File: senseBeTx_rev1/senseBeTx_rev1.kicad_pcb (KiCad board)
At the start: 2 copper layers, 40 x 80 mm, 37 parts, among them J1 Audio-Jack-4_1Switches, P1 CONN_02X05, Q1 TSM2301, Q2 Q_NMOS_DGS, Q3 Q_NMOS_DGS, Q4 Q_NMOS_DGS, Q5 Q_NMOS_DGS, Q6 Q_NMOS_DGS, Q7 Q_NMOS_DGS, Q8 Q_NMOS_DGS, SW1 SW_Push_Dual, U1 STM32L011F3Px, Y1 Crystal

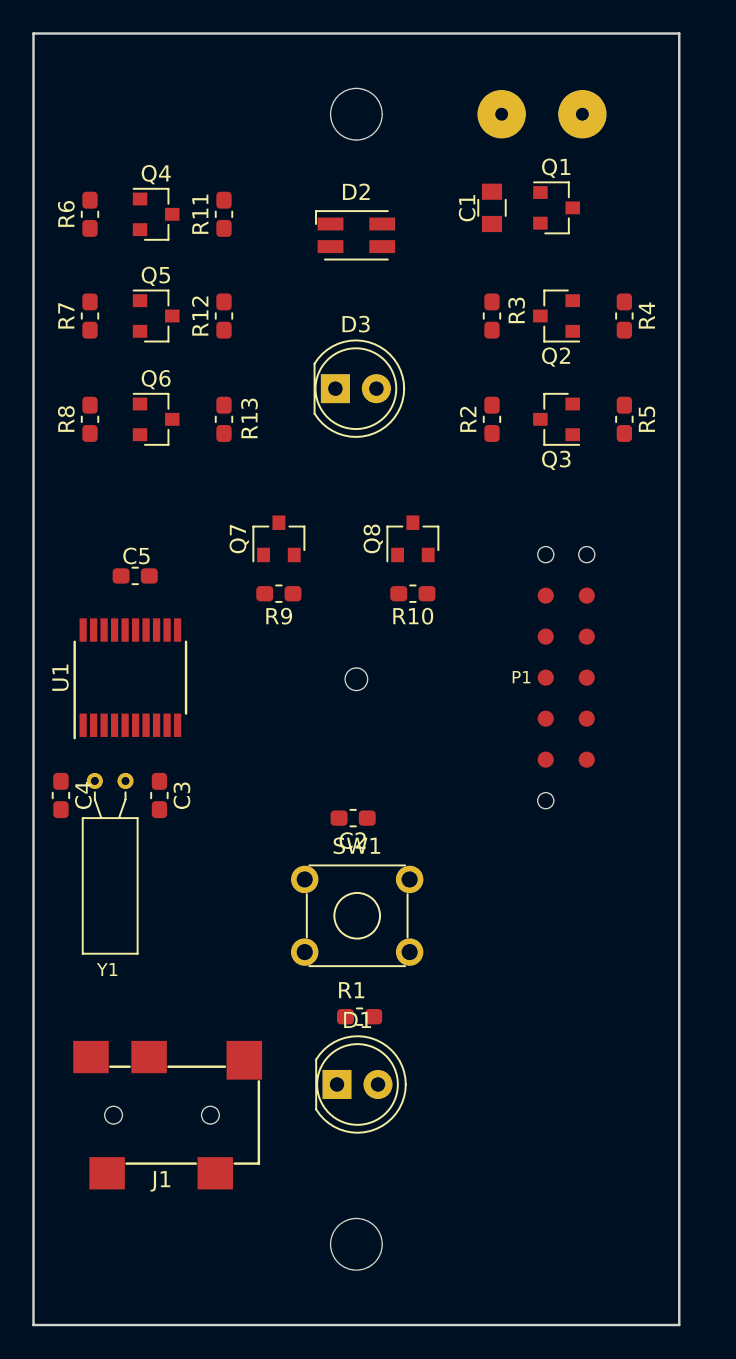
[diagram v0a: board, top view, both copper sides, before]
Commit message: Adds schematic files with minor changes, completed PCB files, and Gerber files for manufacturing
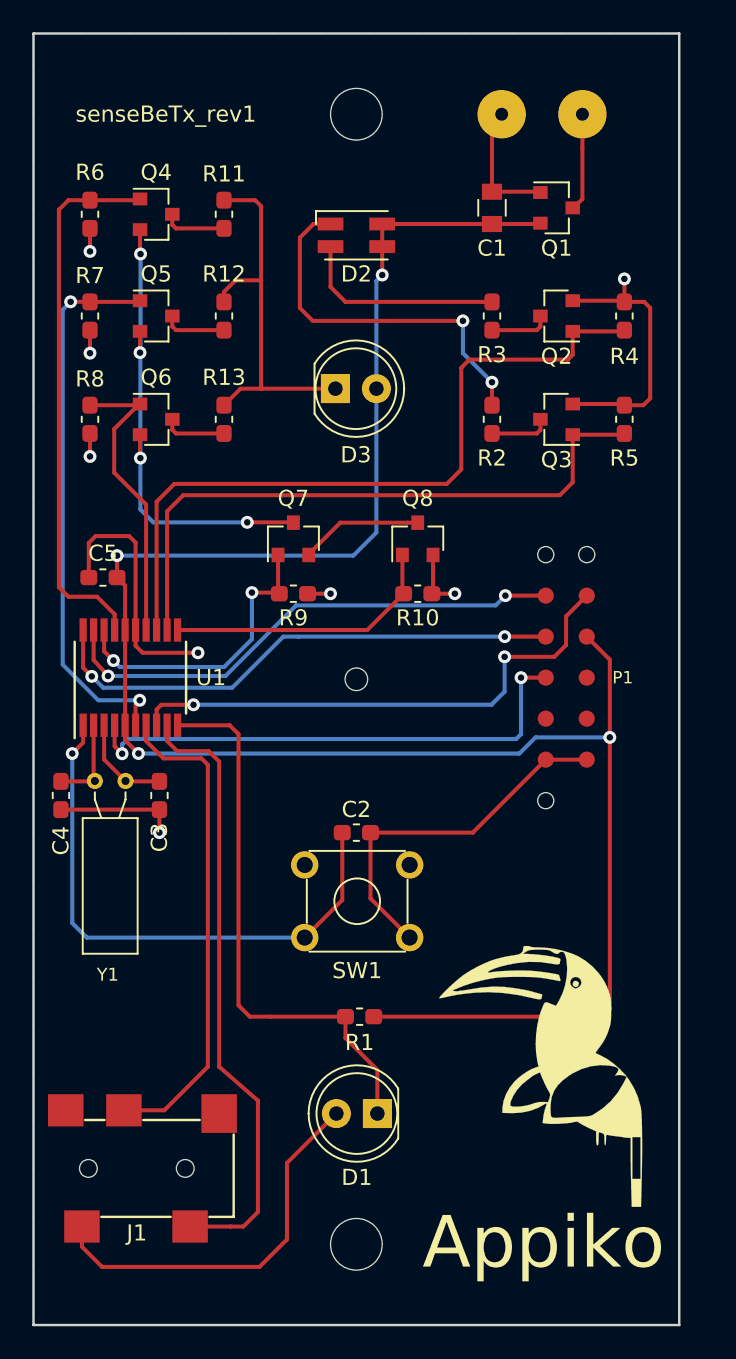
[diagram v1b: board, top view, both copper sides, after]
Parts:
- added G***: LOGO, senseBeTx_rev1_fp:LOGO, F.Cu at (44.4, 181.6)
- Q1: value TSM2301 -> SI2301
- Q2, Q3, Q4, Q5, Q6, Q7, Q8: value Q_NMOS_DGS -> SI2302
- moved SW1 7.43 mm to (36.3, 173.0), turned to 180 degrees
- moved J1 3.65 mm to (13.4, 187.3)
- moved D1 3.08 mm to (34.3, 183.9), turned to 180 degrees
- moved C5 2.00 mm to (17.3, 150.7), turned to 0 degrees
- moved C2 0.92 mm to (33.0, 166.5), turned to 0 degrees
- moved Q7 0.90 mm to (29.1, 148.3)
- moved R9 0.90 mm to (29.1, 151.7)
- moved Q8 0.30 mm to (36.8, 148.3)
- moved R10 0.30 mm to (36.8, 151.7)
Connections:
- C4 pad 1: Net-(C4-Pad1) -> /RCC_OSC32_IN
- Y1 pad 1: Net-(C4-Pad1) -> /RCC_OSC32_IN
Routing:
- net VDD: track 0.00 -> 126.7 mm, vias 0 -> 4
- net GND: track 0.00 -> 105.0 mm, vias 0 -> 8
- net /LED_GREEN: track 0.00 -> 45.9 mm
- net /LED_RED: track 0.00 -> 39.4 mm
- net /LPUART1_RX: track 0.00 -> 38.3 mm
- net /BUTTON: track 0.00 -> 34.8 mm, vias 0 -> 1
- net /LIGHT_SENSE: track 0.00 -> 34.5 mm
- net /LEDIR_PWR2: track 0.00 -> 34.3 mm, vias 0 -> 2
- net /LEDIR_PWR1: track 0.00 -> 33.8 mm
- net /USART2_TX: track 0.00 -> 32.9 mm, vias 0 -> 2
- net /SYS_SWDCLK: track 0.00 -> 32.8 mm, vias 0 -> 2
- net /RESET: track 0.00 -> 32.5 mm, vias 0 -> 2
- net /SYS_SWDIO: track 0.00 -> 32.4 mm, vias 0 -> 2
- net /LPUART1_TX: track 0.00 -> 30.4 mm
- net /R_CNTRL: track 0.00 -> 30.0 mm, vias 0 -> 4
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- added copper zone on B.Cu, net GND
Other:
- board text added: "senseBeTx_rev1"

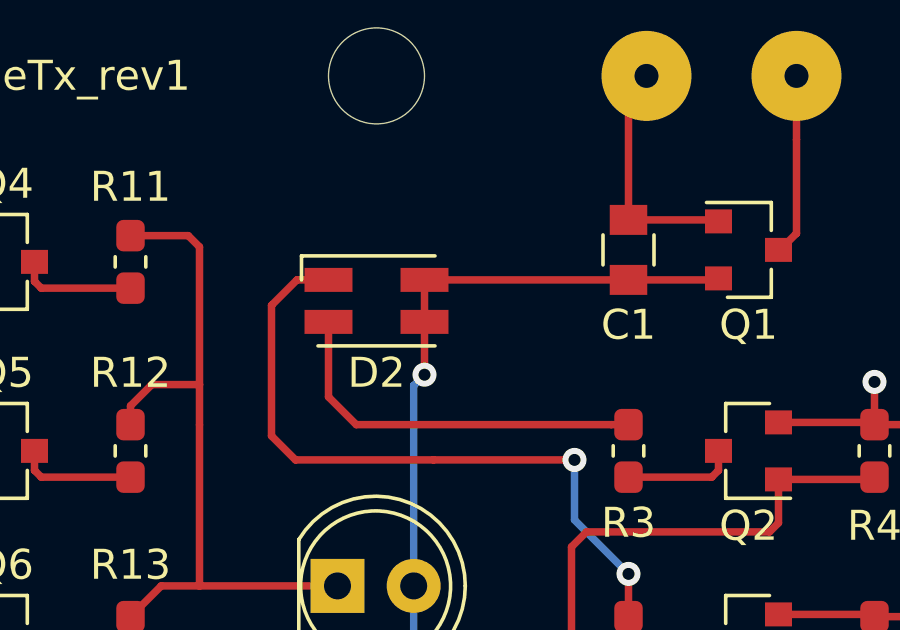
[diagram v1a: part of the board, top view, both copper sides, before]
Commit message: LED in the design is changed to part no. KPTBD-3216SURKCGKC, updated in schematic and PCB
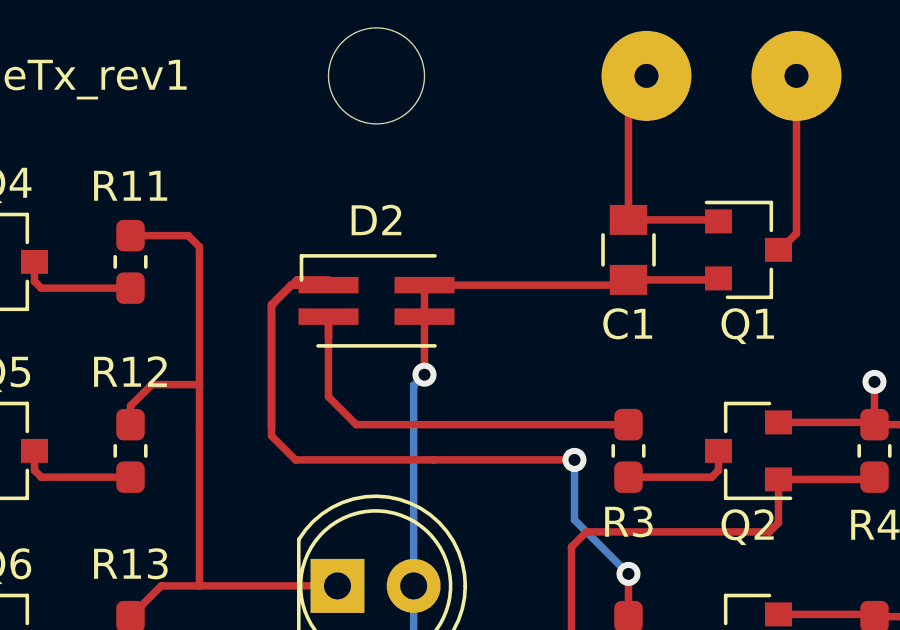
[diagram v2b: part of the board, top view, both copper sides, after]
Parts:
- D2: value APBD3224SURKCGKC-F01 -> KPTBD-3216SURKCGKC; footprint senseBeTx_rev1_fp:LED_APBD3224SURKCGKC-F01 -> senseBeTx_rev1_fp:LED_KPTBD-3216SURKCGKC
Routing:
- net Net-(D2-Pad2): track 23.0 -> 29.2 mm
- net Net-(D2-Pad4): track 12.9 -> 13.6 mm
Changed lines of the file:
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@@
     (thickness 1.6)
     (drawings 9)
-    (tracks 295)
+    (tracks 302)
     (zones 0)
     (modules 38)
@@
       (net 2 GND))
     (model ${KISYS3DMOD}/LED_THT.3dshapes/LED_D5.0mm.wrl
-      (at (xyz 0 0 0))
-      (scale (xyz 1 1 1))
-      (rotate (xyz 0 0 0))
-    )
-  )
-  (module senseBeTx_rev1_fp:LED_APBD3224SURKCGKC-F01 locked (layer F.Cu)
-    (at 33 129.5)
-    (descr https://docs.broadcom.com/docs/AV02-4186EN)
-    (tags "LED Avago PLCC-4 ASMB-MTB0-0A3A2")
-    (attr smd)
-    (fp_text reference D2 (at 0 2.4) (layer F.SilkS)
-      (effects (font (size 1 1) (thickness 0.15)))
-    )
-    (fp_text value APBD3224SURKCGKC-F01 (at 0 2.65) (layer F.Fab)
-      (effects (font (size 1 1) (thickness 0.15)))
-    )
-    (fp_text user %R (at -3.7 0.2) (layer F.Fab)
-      (effects (font (size 0.5 0.5) (thickness 0.075)))
-    )
-    (fp_line (start -0.6 -1.4) (end -1.6 -0.4) (layer F.Fab) (width 0.1))
-    (fp_line (start -1.6 -1.4) (end -1.6 1.4) (layer F.Fab) (width 0.1))
-    (fp_line (start -1.6 1.4) (end 1.6 1.4) (layer F.Fab) (width 0.1))
-    (fp_line (start 1.6 1.4) (end 1.6 -1.4) (layer F.Fab) (width 0.1))
-    (fp_line (start 1.6 -1.4) (end -1.6 -1.4) (layer F.Fab) (width 0.1))
-    (fp_line (start -2.5 -0.7) (end -2.5 -1.5) (layer F.SilkS) (width 0.12))
-    (fp_line (start -2.500044 -1.5) (end 1.95 -1.5) (layer F.SilkS) (width 0.12))
-    (fp_line (start -1.95 1.5) (end 1.95 1.5) (layer F.SilkS) (width 0.12))
-    (fp_line (start -2.5 -1.65) (end 2.5 -1.65) (layer F.CrtYd) (width 0.05))
-    (fp_line (start -2.5 -1.65) (end -2.5 1.65) (layer F.CrtYd) (width 0.05))
-    (fp_line (start 2.5 1.65) (end 2.5 -1.65) (layer F.CrtYd) (width 0.05))
-    (fp_line (start 2.5 1.65) (end -2.5 1.65) (layer F.CrtYd) (width 0.05))
-    (fp_circle (center 0 0) (end 1.12 0) (layer F.Fab) (width 0.1))
-    (pad 2 smd rect (at -1.6 -0.7) (size 1.6 0.8) (layers F.Cu F.Paste F.Mask)
-      (net 8 "Net-(D2-Pad2)"))
-    (pad 1 smd rect (at 1.6 -0.7) (size 1.6 0.8) (layers F.Cu F.Paste F.Mask)
-      (net 3 VDD))
-    (pad 3 smd rect (at 1.6 0.7) (size 1.6 0.8) (layers F.Cu F.Paste F.Mask)
-      (net 3 VDD))
-    (pad 4 smd rect (at -1.6 0.7) (size 1.6 0.8) (layers F.Cu F.Paste F.Mask)
-      (net 9 "Net-(D2-Pad4)"))
-    (model ${KISYS3DMOD}/LED_SMD.3dshapes/LED_Avago_PLCC4_3.2x2.8mm_CW.wrl
       (at (xyz 0 0 0))
       (scale (xyz 1 1 1))
@@
     )
   )
+  (module senseBeTx_rev1_fp:LED_KPTBD-3216SURKCGKC locked (layer F.Cu)
+    (at 33 129.5)
+    (descr https://docs.broadcom.com/docs/AV02-4186EN)
+    (tags "LED Avago PLCC-4 ASMB-MTB0-0A3A2")
+    (attr smd)
+    (fp_text reference D2 (at 0 -2.65) (layer F.SilkS)
+      (effects (font (size 1 1) (thickness 0.15)))
+    )
+    (fp_text value KPTBD-3216SURKCGKC (at 0 2.65) (layer F.Fab)
+      (effects (font (size 1 1) (thickness 0.15)))
+    )
+    (fp_text user %R (at 0 0) (layer F.Fab)
+      (effects (font (size 0.5 0.5) (thickness 0.075)))
+    )
+    (fp_line (start -0.6 -1.4) (end -1.6 -0.4) (layer F.Fab) (width 0.1))
+    (fp_line (start -1.6 -1.4) (end -1.6 1.4) (layer F.Fab) (width 0.1))
+    (fp_line (start -1.6 1.4) (end 1.6 1.4) (layer F.Fab) (width 0.1))
+    (fp_line (start 1.6 1.4) (end 1.6 -1.4) (layer F.Fab) (width 0.1))
+    (fp_line (start 1.6 -1.4) (end -1.6 -1.4) (layer F.Fab) (width 0.1))
+    (fp_line (start -2.5 -0.7) (end -2.5 -1.5) (layer F.SilkS) (width 0.12))
+    (fp_line (start -2.500044 -1.5) (end 1.95 -1.5) (layer F.SilkS) (width 0.12))
+    (fp_line (start -1.95 1.5) (end 1.95 1.5) (layer F.SilkS) (width 0.12))
+    (fp_line (start -2.5 -1.65) (end 2.5 -1.65) (layer F.CrtYd) (width 0.05))
+    (fp_line (start -2.5 -1.65) (end -2.5 1.65) (layer F.CrtYd) (width 0.05))
+    (fp_line (start 2.5 1.65) (end 2.5 -1.65) (layer F.CrtYd) (width 0.05))
+    (fp_line (start 2.5 1.65) (end -2.5 1.65) (layer F.CrtYd) (width 0.05))
+    (fp_circle (center 0 0) (end 1.12 0) (layer F.Fab) (width 0.1))
+    (pad 2 smd rect (at -1.6 -0.525) (size 2 0.55) (layers F.Cu F.Paste F.Mask)
+      (net 8 "Net-(D2-Pad2)"))
+    (pad 1 smd rect (at 1.6 -0.525) (size 2 0.55) (layers F.Cu F.Paste F.Mask)
+      (net 3 VDD))
+    (pad 3 smd rect (at 1.6 0.525) (size 2 0.55) (layers F.Cu F.Paste F.Mask)
+      (net 3 VDD))
+    (pad 4 smd rect (at -1.6 0.525) (size 2 0.55) (layers F.Cu F.Paste F.Mask)
+      (net 9 "Net-(D2-Pad4)"))
+    (model ${KISYS3DMOD}/LED_SMD.3dshapes/LED_Avago_PLCC4_3.2x2.8mm_CW.wrl
+      (at (xyz 0 0 0))
+      (scale (xyz 1 1 1))
+      (rotate (xyz 0 0 0))
+    )
+  )
   (gr_text senseBeTx_rev1 (at 21.2 122) (layer F.SilkS)
     (effects (font (size 1 1) (thickness 0.15)))
@@
   (segment (start 44.35 128.8) (end 44.4 128.75) (width 0.25) (layer F.Cu) (net 3))
   (segment (start 41.4 128.8) (end 44.35 128.8) (width 0.25) (layer F.Cu) (net 3))
-  (segment (start 41.4 128.8) (end 34.6 128.8) (width 0.25) (layer F.Cu) (net 3))
-  (segment (start 34.6 128.8) (end 34.6 130.2) (width 0.25) (layer F.Cu) (net 3))
   (via (at 34.6 131.96) (size 0.8) (drill 0.4) (layers F.Cu B.Cu) (net 3))
   (segment (start 34.24 132.32) (end 34.6 131.96) (width 0.25) (layer B.Cu) (net 3))
   (segment (start 34.24 139) (end 34.24 132.32) (width 0.25) (layer B.Cu) (net 3))
-  (segment (start 34.6 131.96) (end 34.6 130.2) (width 0.25) (layer F.Cu) (net 3))
   (segment (start 34.075 177.9) (end 48.23 177.9) (width 0.25) (layer F.Cu) (net 3))
   (segment (start 48.7 177.43) (end 48.7 160.6) (width 0.25) (layer F.Cu) (net 3))
@@
   (segment (start 32.81 149.34) (end 18.18 149.34) (width 0.25) (layer B.Cu) (net 3))
   (segment (start 34.24 147.91) (end 32.81 149.34) (width 0.25) (layer B.Cu) (net 3))
+  (segment (start 41.225 128.975) (end 41.4 128.8) (width 0.25) (layer F.Cu) (net 3))
+  (segment (start 34.6 128.975) (end 41.225 128.975) (width 0.25) (layer F.Cu) (net 3))
+  (segment (start 34.6 128.975) (end 34.6 130.025) (width 0.25) (layer F.Cu) (net 3))
+  (segment (start 34.6 130.025) (end 34.6 131.96) (width 0.25) (layer F.Cu) (net 3))
   (via (at 15.4 161.6) (size 0.8) (drill 0.4) (layers F.Cu B.Cu) (net 4))
   (segment (start 16.075 160.925) (end 15.4 161.6) (width 0.25) (layer F.Cu) (net 4))
@@
   (segment (start 39.6 134.8) (end 39.6 136.8) (width 0.25) (layer B.Cu) (net 8))
   (segment (start 41.4 138.6) (end 41.4 140.025) (width 0.25) (layer F.Cu) (net 8))
-  (segment (start 29.5 129.65) (end 29.5 134) (width 0.25) (layer F.Cu) (net 8))
   (segment (start 30.3 134.8) (end 34.9 134.8) (width 0.25) (layer F.Cu) (net 8))
   (segment (start 29.5 134) (end 30.3 134.8) (width 0.25) (layer F.Cu) (net 8))
   (segment (start 34.9 134.8) (end 39.6 134.8) (width 0.25) (layer F.Cu) (net 8))
+  (segment (start 29.5 129.625) (end 29.5 133.7) (width 0.25) (layer F.Cu) (net 8))
+  (segment (start 30.15 128.975) (end 29.5 129.625) (width 0.25) (layer F.Cu) (net 8))
+  (segment (start 31.4 128.975) (end 30.15 128.975) (width 0.25) (layer F.Cu) (net 8))
+  (segment (start 29.5 129.65) (end 29.5 133.7) (width 0.25) (layer F.Cu) (net 8))
+  (segment (start 29.5 133.7) (end 29.5 134) (width 0.25) (layer F.Cu) (net 8))
   (segment (start 32.325 133.625) (end 40.825 133.625) (width 0.25) (layer F.Cu) (net 9))
   (segment (start 31.4 132.7) (end 32.325 133.625) (width 0.25) (layer F.Cu) (net 9))
   (segment (start 40.825 133.625) (end 41.4 133.625) (width 0.25) (layer F.Cu) (net 9))
-  (segment (start 31.4 130.2) (end 31.4 132.7) (width 0.25) (layer F.Cu) (net 9))
+  (segment (start 31.4 130.025) (end 31.4 130.7) (width 0.25) (layer F.Cu) (net 9))
+  (segment (start 31.4 130.7) (end 31.4 132.7) (width 0.25) (layer F.Cu) (net 9))
+  (segment (start 31.4 130.2) (end 31.4 130.7) (width 0.25) (layer F.Cu) (net 9))
   (segment (start 26.725 127.325) (end 24.8 127.325) (width 0.25) (layer F.Cu) (net 10))
   (segment (start 27.1 127.7) (end 26.725 127.325) (width 0.25) (layer F.Cu) (net 10))
